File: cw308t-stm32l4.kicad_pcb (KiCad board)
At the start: 2 copper layers, 53 x 65 mm, 18 parts, among them J1 CW308T_CONNBOARD, J2 Conn_02x03_Odd_Even, U1 STM32L432KCUx

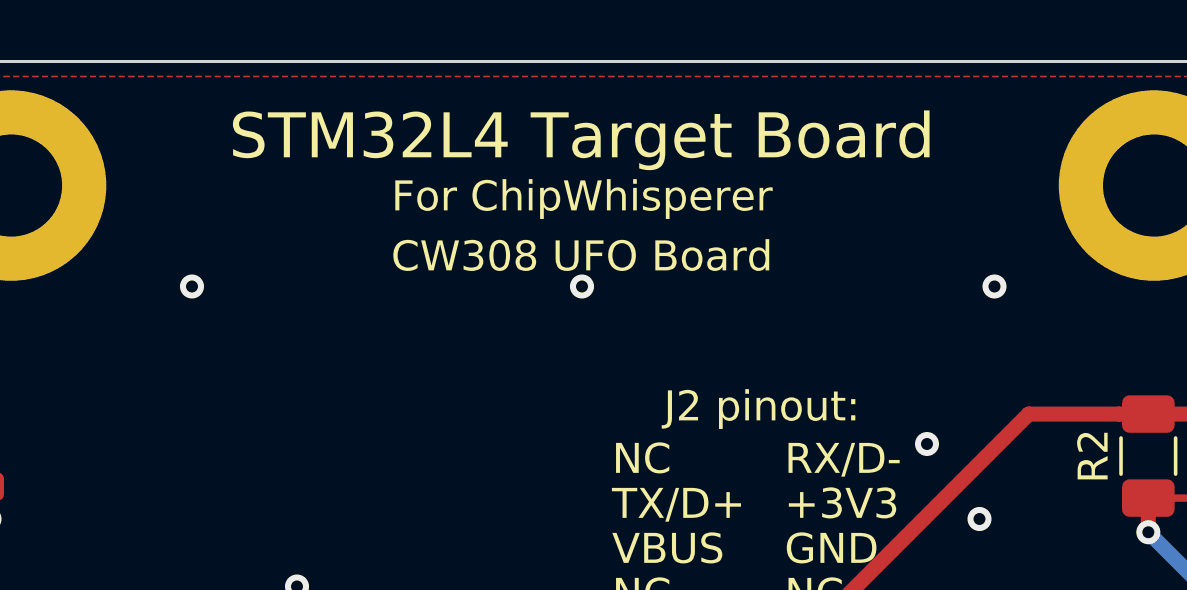
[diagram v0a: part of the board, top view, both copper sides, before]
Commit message: Add license to silkscreen
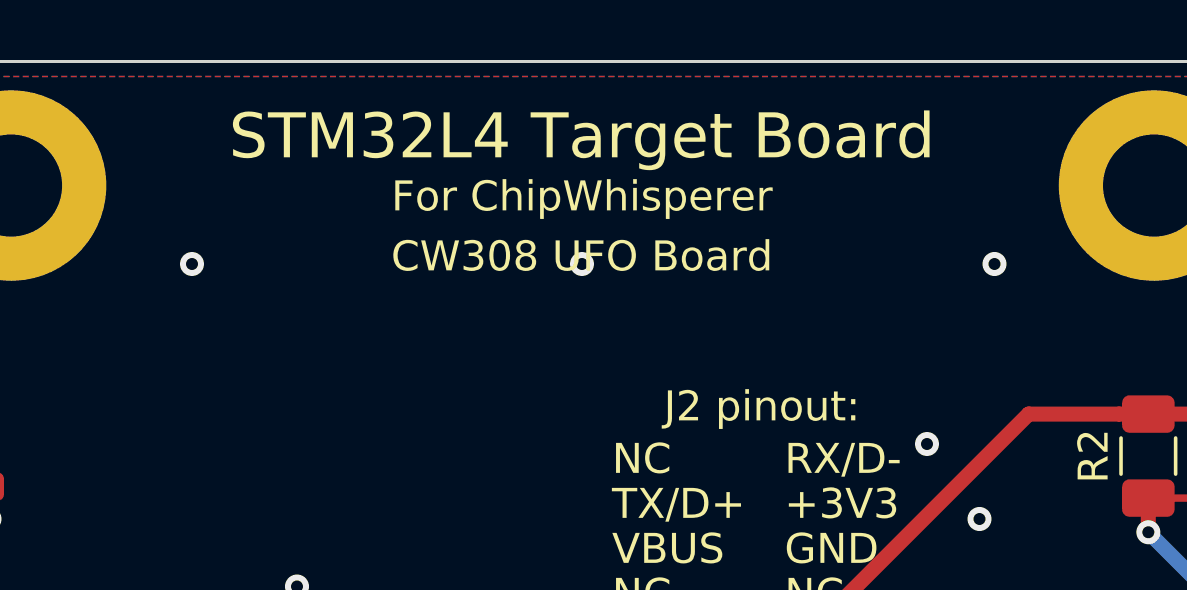
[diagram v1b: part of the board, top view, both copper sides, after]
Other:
- board text added: "Licensed under CERN OHL v.1.2 or later"
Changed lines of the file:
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@@
   (general
     (thickness 1.6)
-    (drawings 24)
+    (drawings 25)
     (tracks 503)
     (zones 0)
@@
     )
   )
+  (gr_text "Licensed under CERN OHL v.1.2 or later" (at 148 67.75) (layer B.SilkS)
+    (effects (font (size 1 1) (thickness 0.15)) (justify mirror))
+  )
   (gr_text "© 2019 mickdermack, aveexy" (at 148.25 63.25) (layer B.SilkS)
     (effects (font (size 1 1) (thickness 0.15)) (justify mirror))
@@
   (segment (start 169.210201 89.184) (end 168.5 89.184) (width 0.25) (layer F.Cu) (net 1))
   (segment (start 169.75 88.644201) (end 169.210201 89.184) (width 0.25) (layer F.Cu) (net 1))
-  (via (at 161.75 67.5) (size 0.8) (drill 0.4) (layers F.Cu B.Cu) (net 2))
+  (via (at 161.75 66.75) (size 0.8) (drill 0.4) (layers F.Cu B.Cu) (net 2))
   (via (at 145.034 96.012) (size 0.8) (drill 0.4) (layers F.Cu B.Cu) (net 2))
   (segment (start 146.1525 95.73) (end 145.316 95.73) (width 0.25) (layer F.Cu) (net 2))
@@
   (via (at 159 95.5) (size 0.8) (drill 0.4) (layers F.Cu B.Cu) (net 2))
   (via (at 166.878 94.996) (size 0.8) (drill 0.4) (layers F.Cu B.Cu) (net 2))
-  (via (at 135 67.5) (size 0.8) (drill 0.4) (layers F.Cu B.Cu) (net 2))
-  (via (at 148 67.5) (size 0.8) (drill 0.4) (layers F.Cu B.Cu) (net 2))
+  (via (at 135 66.75) (size 0.8) (drill 0.4) (layers F.Cu B.Cu) (net 2))
+  (via (at 148 66.75) (size 0.8) (drill 0.4) (layers F.Cu B.Cu) (net 2))
   (via (at 161.25 75.25) (size 0.8) (drill 0.4) (layers F.Cu B.Cu) (net 2))
   (via (at 155.5 81.25) (size 0.8) (drill 0.4) (layers F.Cu B.Cu) (net 2))

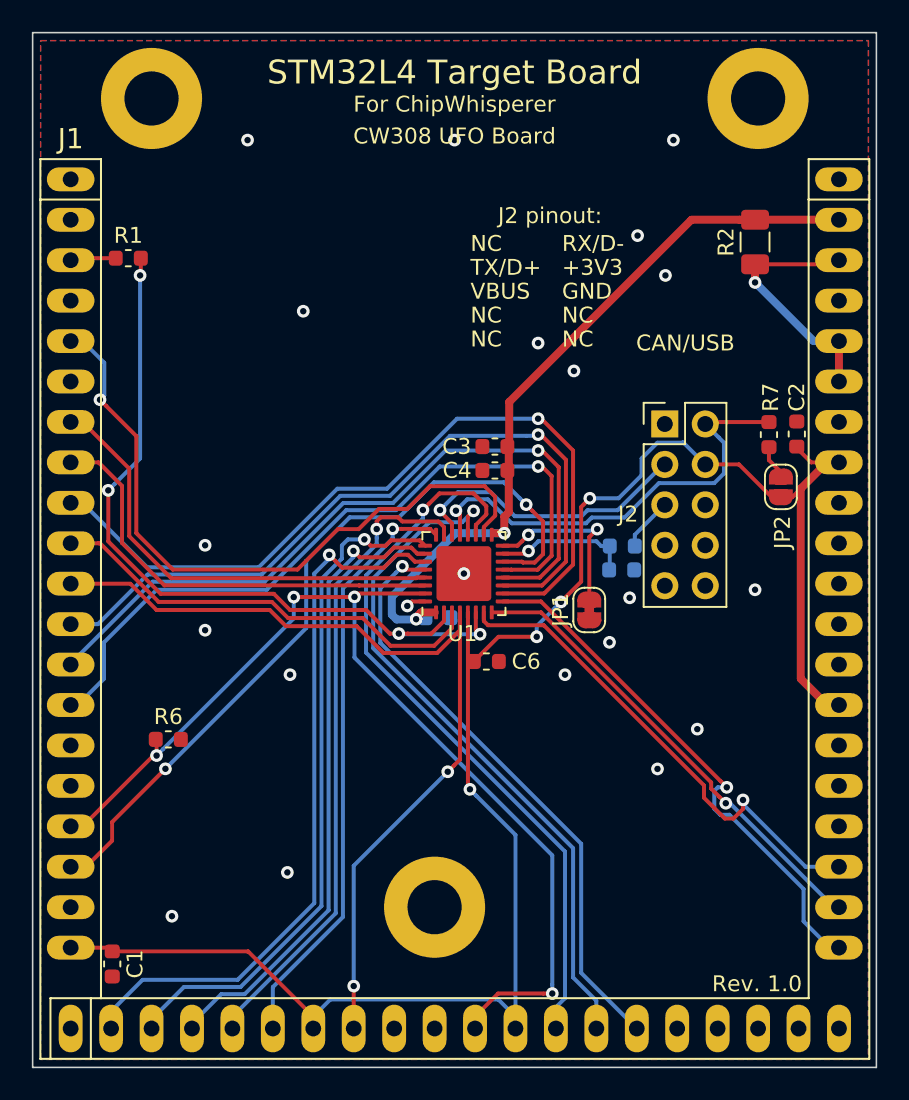
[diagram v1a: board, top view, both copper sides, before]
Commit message: Larger silkscreen stuff, fixes #2
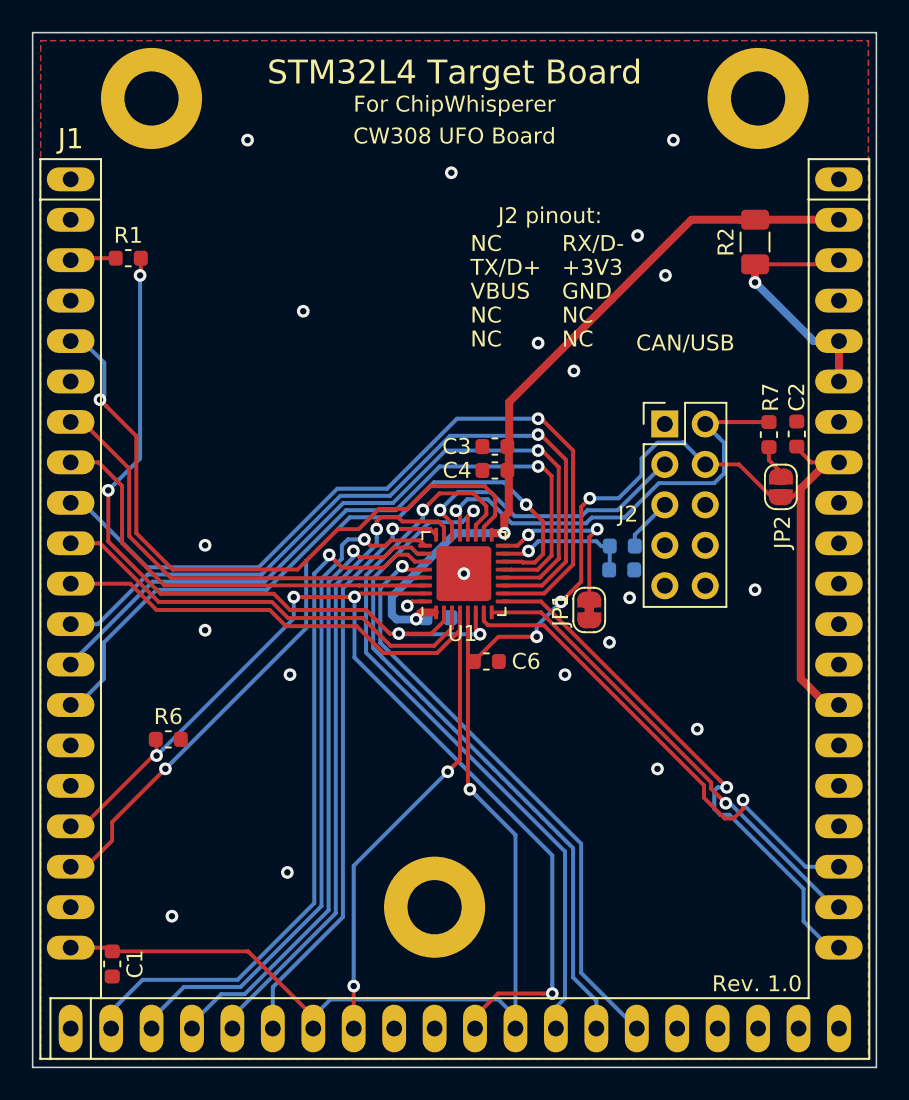
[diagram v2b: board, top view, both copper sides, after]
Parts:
- REF**: value OSHW-Logo_5.7x6mm_SilkScreen -> OSHW-Logo_7.5x8mm_SilkScreen; footprint Symbol:OSHW-Logo_5.7x6mm_SilkScreen -> Symbol:OSHW-Logo_7.5x8mm_SilkScreen

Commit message: Swap UART, I2C (see #1); add more visible pin 1 marker for STM32
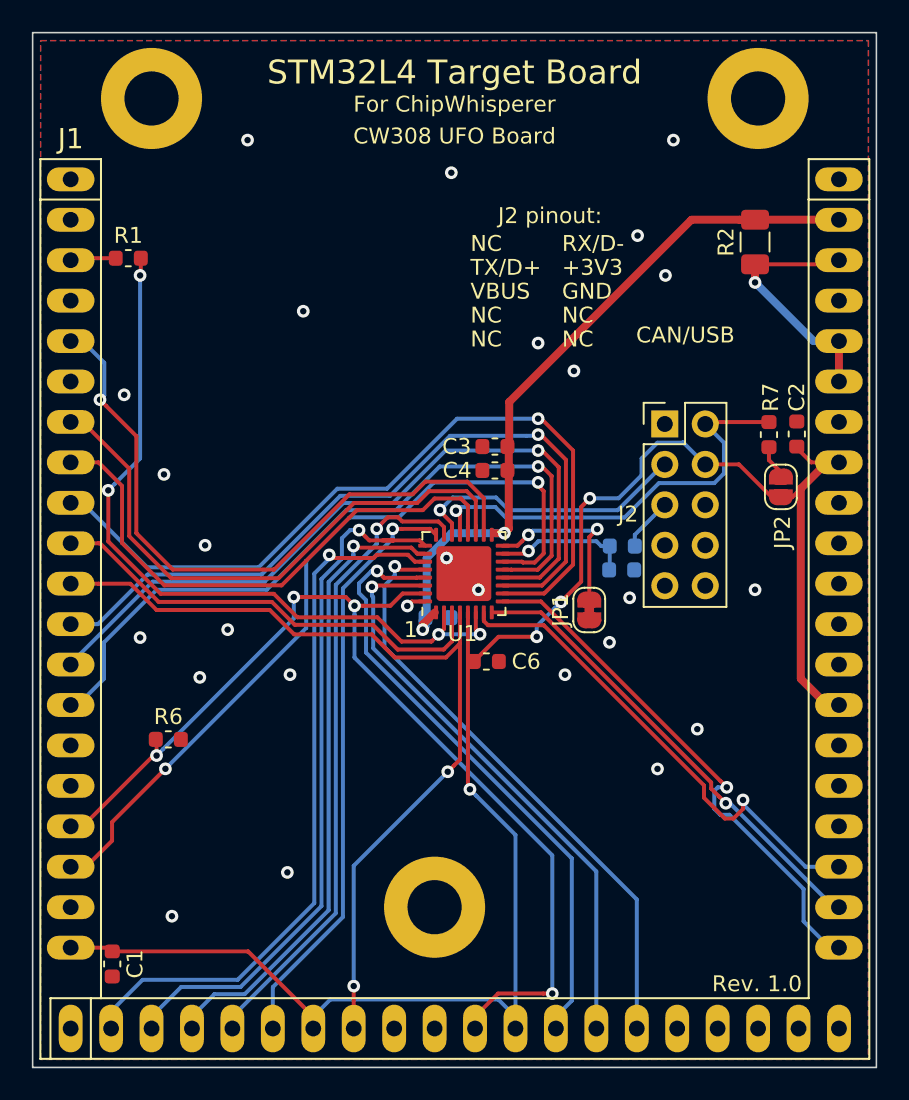
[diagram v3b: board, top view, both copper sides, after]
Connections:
- U1 pad 19: /I2C_SCL -> /TX
- U1 pad 20: /I2C_SDA -> /RX
- U1 pad 29: /TX -> /I2C_SCL
- U1 pad 30: /RX -> /I2C_SDA
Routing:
- net /TX: track 28.8 -> 36.7 mm
- net /I2C_SCL: track 46.3 -> 38.6 mm
- net /RX: track 27.6 -> 34.5 mm
- net /I2C_SDA: track 44.5 -> 37.7 mm
- net /CLKI: track 49.6 -> 47.8 mm
- net Net-(C3-Pad1): track 48.3 -> 46.7 mm
- net /NRST: track 56.9 -> 55.6 mm
- net /TDI: track 43.2 -> 44.4 mm
- net /SPI_SS: track 49.7 -> 50.9 mm
- net /CLKO: track 43.1 -> 42.2 mm
- net /CAN_RX: track 28.3 -> 27.6 mm
- net /GPIO4: track 28.1 -> 28.7 mm
- net /CAN_TX: track 18.4 -> 17.8 mm
- net /TRST: track 45.8 -> 45.3 mm
- net GND: vias 21 -> 26
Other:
- board text added: "1"

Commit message: Swap GPIO3 and SPI_SS (see #1)
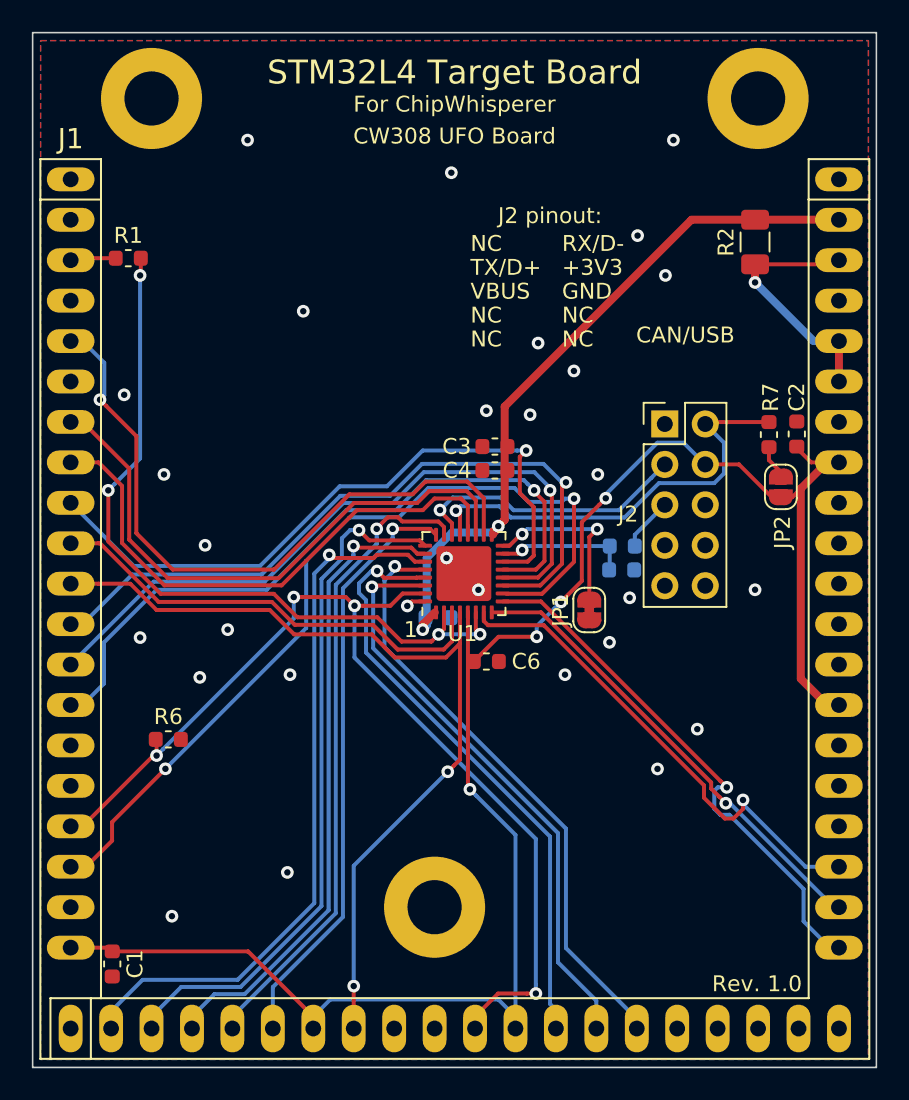
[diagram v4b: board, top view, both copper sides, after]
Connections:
- U1 pad 10: /GPIO3 -> /SPI_SS
- U1 pad 14: /SPI_SS -> /GPIO3
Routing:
- net /GPIO3: track 50.3 -> 42.5 mm
- net /SPI_SS: track 50.9 -> 55.2 mm
- net /SPI_MISO: track 46.5 -> 43.8 mm
- net /SPI_SCLK: track 47.5 -> 45.3 mm
- net /SPI_MOSI: track 46.4 -> 44.3 mm
- net /BOOT0: track 67.2 -> 65.8 mm
- net Net-(C3-Pad1): track 46.7 -> 45.6 mm
- net VCC: track 115.6 -> 114.5 mm
- net /I2C_SCL: track 38.6 -> 37.7 mm
- net /TDI: track 44.4 -> 43.8 mm
- net GND: vias 26 -> 29

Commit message: Bump schematic and board revision
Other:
- board text added: "Rev. 2.0"
- board text removed: "Rev. 1.0"
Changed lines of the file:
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@@
   )
   (setup
-    (last_trace_width 0.5)
+    (last_trace_width 0.25)
     (user_trace_width 0.5)
     (trace_clearance 0.2)
@@
     (effects (font (size 1 1) (thickness 0.2)) (justify mirror))
   )
-  (gr_text "Rev. 1.0" (at 167 119.75) (layer F.SilkS)
+  (gr_text "Rev. 2.0" (at 167 119.75) (layer F.SilkS)
     (effects (font (size 1 1) (thickness 0.2)))
   )
